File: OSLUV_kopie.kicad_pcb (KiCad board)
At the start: 4 copper layers, 110 x 90 mm, 190 parts, among them IC1 NCP12510ASN65T1G, IC2 SFH6156-3, IC3 INA210, IC4 AP63300WU-7, IC5 AP63300WU-7, IC6 STM32G071KBT6, IC7 TLV9001IDBVR, IC8 FAN3100TSX, IC9 TLV1821, J1 B08B-XASK-1-A_LF__SN_, J2 TC2050-IDC, J3 BM02B-SRSS-TB_LF__SN_, J4 BM02B-SRSS-TB_LF__SN_, J5 640445-2, J6 640445-2, J7 B5P-VH, Q1 STD3NK80ZT4, Q2 BAT847B, Q3 BSS138, Q4 BC807, T1 750343466, T4 NMOS_GDS-KS_SMD, U1 OPA2356AIDGKR, U2 AZ431LANTR

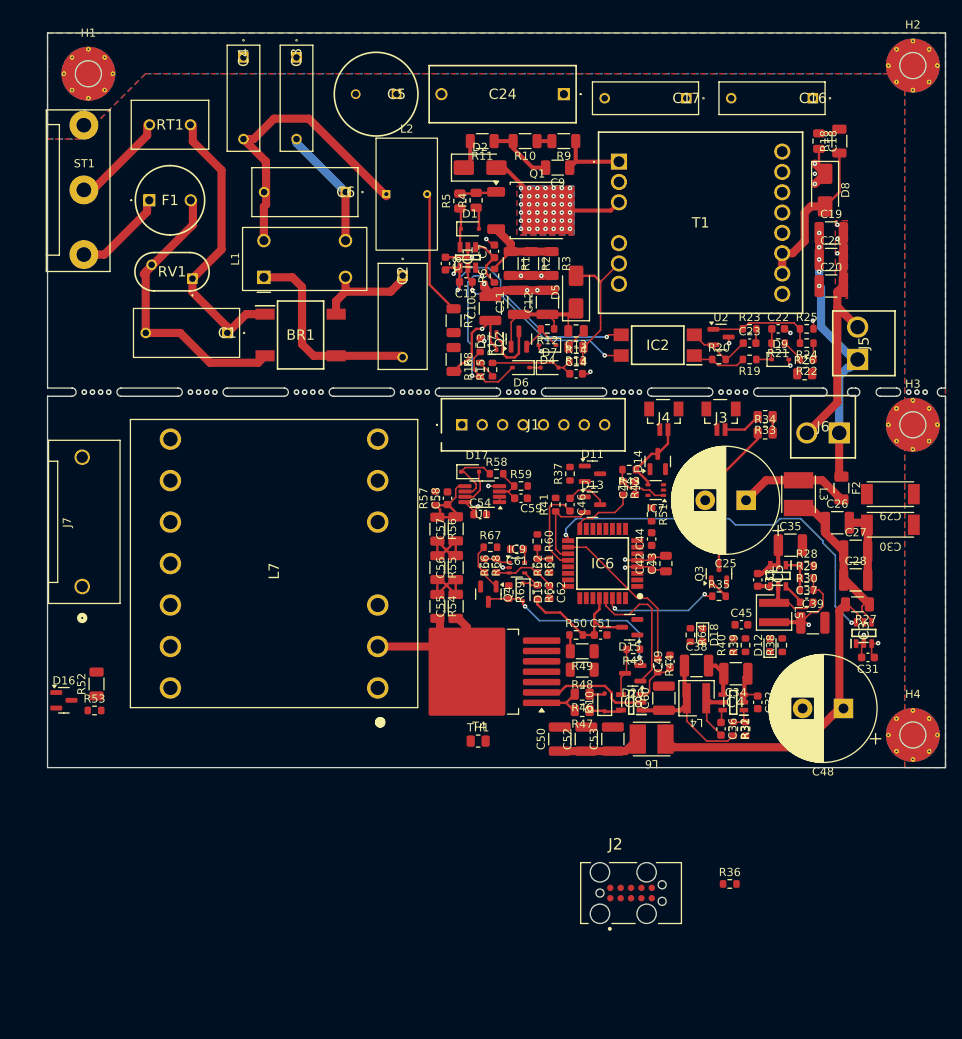
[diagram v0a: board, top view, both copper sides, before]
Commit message: new transformer, top layer only
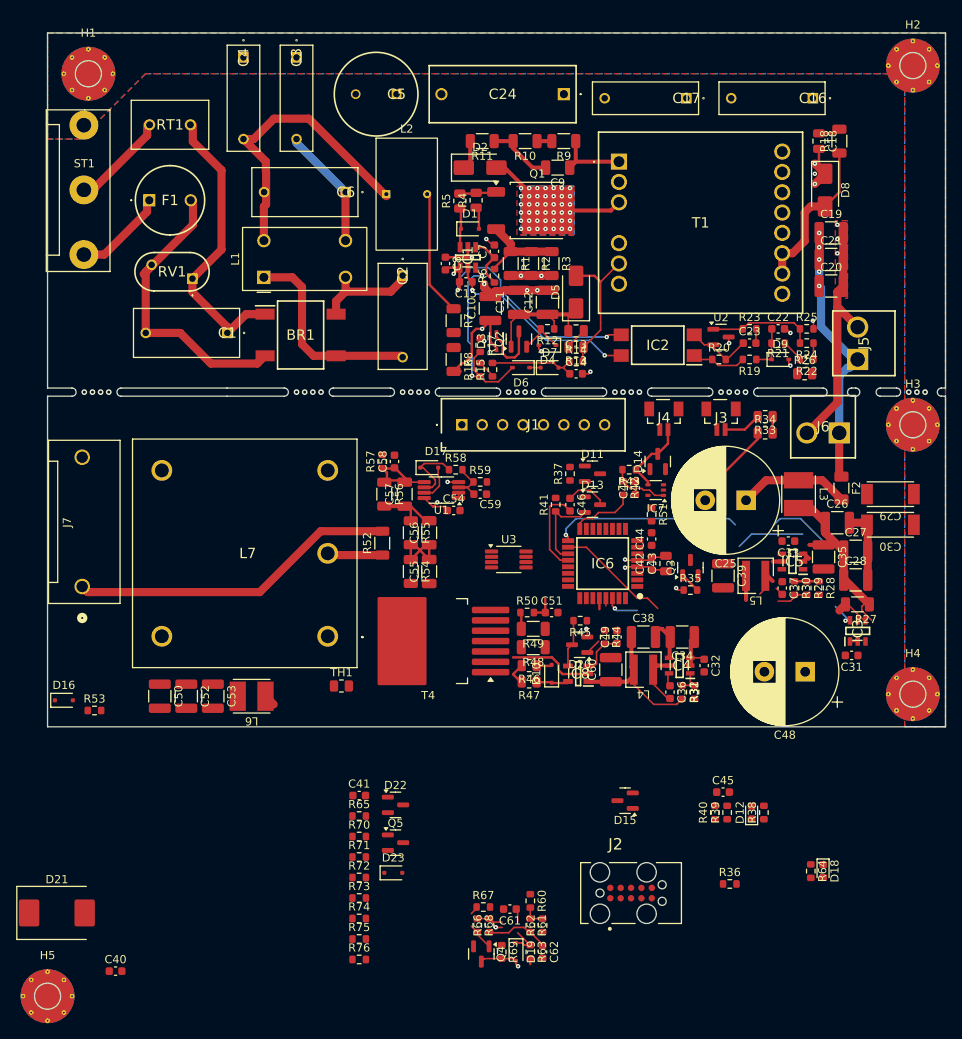
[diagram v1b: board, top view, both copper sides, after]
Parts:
- removed IC9: TLV1821, Package_TO_SOT_SMD:SOT-353_SC-70-5
- added C40: 47n 0603, Capacitor_SMD:C_0603_1608Metric, F.Cu at (58.3, 164.9)
- added C41: 100n 0603, Capacitor_SMD:C_0603_1608Metric, F.Cu at (88.2, 143.4)
- added D21: 3KASMC24AHE3, Diode_SMD:D_SMC, F.Cu at (51.1, 157.8)
- added D22: BAS40-04, Package_TO_SOT_SMD:SOT-23, F.Cu at (92.6, 144.6)
- added D23: BAT54J, Diode_SMD:D_SOD-323F, F.Cu at (92.3, 152.9)
- added H5: MountingHole_Pad, Hansmann:Mounting_M3_NPTH_Vias, F.Cu at (50.0, 168.0)
- added Q5: BC807, Package_TO_SOT_SMD:SOT-23, F.Cu at (92.6, 149.2)
- added R65: 10k 0603, Resistor_SMD:R_0603_1608Metric, F.Cu at (88.2, 145.9)
- added R70: 10k 0603, Resistor_SMD:R_0603_1608Metric, F.Cu at (88.2, 148.4)
- added R71: 2k2 0603, Resistor_SMD:R_0603_1608Metric, F.Cu at (88.2, 150.9)
- added R72: 1k 0603, Resistor_SMD:R_0603_1608Metric, F.Cu at (88.2, 153.5)
- added R73: 10k 0603, Resistor_SMD:R_0603_1608Metric, F.Cu at (88.2, 156.0)
- added R74: 100k 0603, Resistor_SMD:R_0603_1608Metric, F.Cu at (88.2, 158.5)
- added R75: 10k 0603, Resistor_SMD:R_0603_1608Metric, F.Cu at (88.2, 161.0)
- added R76: 10k 0603, Resistor_SMD:R_0603_1608Metric, F.Cu at (88.2, 163.5)
- added U3: LM2904, Package_SO:VSSOP-8_3x3mm_P0.65mm, F.Cu at (106.5, 114.5)
- D16: value BAS40-04 -> BAT54J; footprint Package_TO_SOT_SMD:SOT-23 -> Diode_SMD:D_SOD-323F
- L7: value ETD29 -> EF25; footprint Hansmann:B66359B1013T001 -> OSLUV:EF25_outerPinsOnly
- R52: value 1R 1206 -> 82R 1206/MMA
- R53: value 1k 0603 -> 51R 0603
- T4: footprint Hansmann:TO-263-7_TabPin2 -> Hansmann:TO-263-7_TabPin2_HV
- moved C50 49.3 mm to (63.8, 131.2), turned to -90 degrees
- moved C52 49.3 mm to (67.0, 131.2), turned to -90 degrees
- moved C53 49.3 mm to (70.2, 131.2), turned to -90 degrees
- moved L6 49.3 mm to (75.0, 131.2)
- moved C61 44.1 mm to (106.6, 157.3)
- moved C62 44.1 mm to (110.6, 162.6)
- moved D19 44.1 mm to (107.4, 162.6)
- moved Q4 44.1 mm to (103.1, 162.8)
- moved R60 44.1 mm to (109.1, 156.3)
- moved R61 44.1 mm to (109.1, 159.3)
- moved R62 44.1 mm to (110.6, 159.3)
- moved R63 44.1 mm to (109.1, 162.6)
- moved R66 44.1 mm to (104.1, 159.3)
- moved R67 44.1 mm to (103.4, 157.1)
- moved R68 44.1 mm to (102.6, 159.3)
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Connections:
- D16 pad 1: GND -> /excimerDriver/Isense_Lamp
- D16 pad 2: +3V3 -> Net-(D16-A)
- L7 pad 1: unconnected-(L7-Pad1) -> /excimerDriver/lampDriver/HV_Drain
- L7 pad 10: unconnected-(L7-Pad10) -> /excimerDriver/lampDriver/VDC_Trafo
- L7 pad 3: unconnected-(L7-Pad3) -> GND
- L7 pad 5: Net-(L7-Pad5) -> unconnected-(L7-Pad5)
- L7 pad 6: Net-(L7-Pad5) -> /excimerDriver/lampDriver/Lamp_HV
- R53 pad 1: Net-(D16-Pad3) -> Net-(D16-A)
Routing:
- net /excimerDriver/lampDriver/Lamp_GND: track 0.00 -> 40.1 mm
- net /excimerDriver/VDC_power: track 40.1 -> 5.79 mm
- net /excimerDriver/lampDriver/HV_Drain: track 26.7 -> 0.00 mm
- net Net-(D19-A): track 24.7 -> 6.32 mm
- net /excimerDriver/DRV_Mask: track 17.2 -> 2.91 mm
- net /excimerDriver/Isense_MOS: track 17.7 -> 5.19 mm
- net +3V3: track 34.5 -> 24.3 mm, vias 4 -> 2
- net /excimerDriver/lampDriver/VDC_Trafo: track 10.2 -> 0.00 mm
- net /excimerDriver/UV_LED: track 14.3 -> 5.27 mm
- net /excimerDriver/DRV: track 20.3 -> 14.1 mm
- net Net-(Q3-D): track 18.3 -> 12.7 mm
- net /excimerDriver/Isense_In: track 47.4 -> 42.6 mm
- net Net-(D21-K): track 13.7 -> 16.9 mm
- net Net-(T4-G): track 6.54 -> 3.54 mm
- net Net-(IC5-BST): track 2.69 -> 0.18 mm
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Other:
- board size 110 x 90 mm -> 110 x 85 mm
